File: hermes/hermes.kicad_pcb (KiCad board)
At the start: 2 copper layers, 46.5 x 74 mm, 9 parts, among them U1 AHT20, U2 XIAO-RP2040-DIP

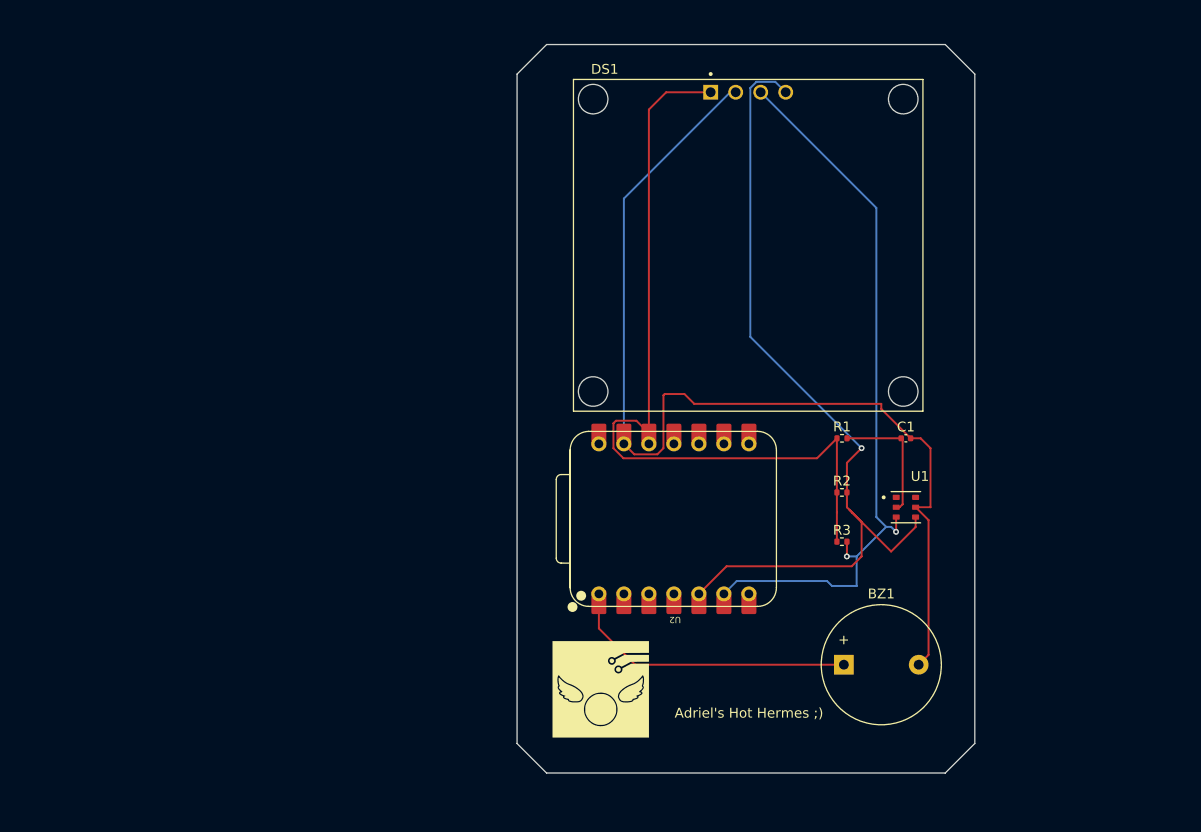
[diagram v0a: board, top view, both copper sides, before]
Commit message: changed some footprints
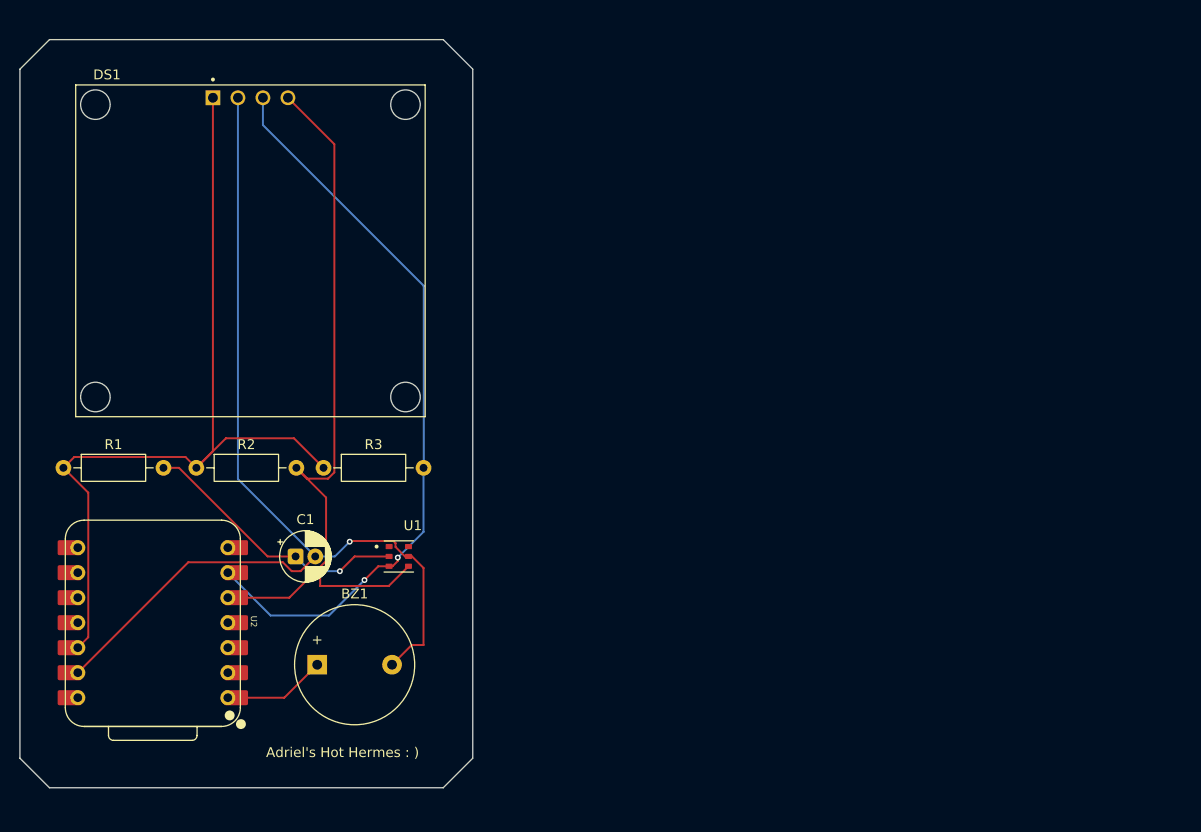
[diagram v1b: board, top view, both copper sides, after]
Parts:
- removed G***: LOGO, hermes:herm-22
- C1: footprint Capacitor_SMD:C_0402_1005Metric -> Capacitor_THT:CP_Radial_D5.0mm_P2.00mm
- R1, R2, R3: footprint Resistor_SMD:R_0402_1005Metric -> Resistor_THT:R_Axial_DIN0207_L6.3mm_D2.5mm_P10.16mm_Horizontal
- moved R1 79.1 mm to (69.4, 93.0)
- moved R2 65.6 mm to (82.9, 93.0)
- moved C1 63.2 mm to (93.0, 102.0)
- moved U2 54.0 mm to (78.5, 108.7), turned to -90 degrees
- moved BZ1 53.5 mm to (95.2, 113.0)
- moved R3 53.2 mm to (95.8, 93.0)
- moved U1 51.8 mm to (103.5, 102.0)
- moved DS1 50.6 mm to (88.4, 71.0)
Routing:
- net buzzer: track 29.9 -> 10.5 mm
- net Net-(U1-VDD): track 13.0 -> 27.9 mm, vias 0 -> 1
- net Net-(DS1-SDA): track 86.4 -> 77.5 mm, vias 1 -> 0
- net Net-(DS1-VDD): track 83.3 -> 87.9 mm
- net GND: track 105.1 -> 104.5 mm, vias 0 -> 1
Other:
- board size 46.5 x 74 mm -> 46 x 76 mm
- board text added: "Adriel's Hot Hermes : )"
- board text removed: "Adriel's Hot Hermes ;)"

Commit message: done
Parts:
- removed C1: 10u, Capacitor_THT:CP_Radial_D5.0mm_P2.00mm
- removed R1: 330, Resistor_THT:R_Axial_DIN0207_L6.3mm_D2.5mm_P10.16mm_Horizontal
- removed R2, R3: 4.7k, Resistor_THT:R_Axial_DIN0207_L6.3mm_D2.5mm_P10.16mm_Horizontal
- removed U1: AHT20, hermes-footprint:PSON100P300X300X110-6N
- added J1: Conn_01x04_Pin, Connector:FanPinHeader_1x04_P2.54mm_Vertical, F.Cu at (173.7, 98.8)
- moved U2 75.6 mm to (154.0, 112.6), turned to 180 degrees
- moved BZ1 75.5 mm to (170.7, 114.0)
- moved DS1 72.7 mm to (161.1, 67.7)
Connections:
- net Net-(DS1-SCK) renamed SCL
- net Net-(DS1-SDA) renamed SDA
- net Net-(DS1-VDD) renamed VDD
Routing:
- net Net-(U1-VDD): track 27.9 -> 0.00 mm, vias 1 -> 0
- net buzzer: track 10.5 -> 26.9 mm
- net VDD: track 87.9 -> 78.4 mm
- net GND: track 104.5 -> 98.2 mm
- net SDA: track 77.5 -> 82.3 mm
- net SCL: track 76.3 -> 80.6 mm, vias 2 -> 0
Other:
- board size 46 x 76 mm -> 43.5 x 80.5 mm
- board text removed: "Adriel's Hot Hermes : )"

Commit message: made a case
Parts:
- moved U2 3.13 mm to (151.0, 113.5)
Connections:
- J1 pad 1: VDD -> SDA
- J1 pad 2: GND -> SCL
- J1 pad 3: SCL -> GND
- J1 pad 4: SDA -> VDD
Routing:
- net SDA: track 82.3 -> 91.8 mm, vias 0 -> 1
- net buzzer: track 26.9 -> 34.4 mm
- net SCL: track 80.6 -> 87.4 mm, vias 0 -> 2
- net GND: track 98.2 -> 104.7 mm, vias 1 -> 3
- net VDD: track 78.4 -> 77.4 mm
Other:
- board size 43.5 x 80.5 mm -> 44 x 78 mm

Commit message: done again again
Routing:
- net VDD: track 77.4 -> 85.1 mm
- net SCL: track 87.4 -> 85.0 mm
- net buzzer: track 34.4 -> 32.6 mm
- net SDA: track 91.8 -> 90.2 mm
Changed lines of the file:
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@@
-	)
-	(segment
-		(start 159.82 52.105)
-		(end 159.82 83.274206)
-		(width 0.2)
-		(layer "F.Cu")
-		(net 1)
 	)
 	(segment
@@
 	)
 	(segment
+		(start 178.3 96.8)
+		(end 175.22 93.72)
+		(width 0.2)
+		(layer "F.Cu")
+		(net 1)
+	)
+	(segment
 		(start 159.045794 82.5)
 		(end 159.82 83.274206)
@@
 	)
 	(segment
-		(start 177.72 93.72)
-		(end 173.7 93.72)
+		(start 158.5 53.425)
+		(end 158.5 81.954206)
 		(width 0.2)
 		(layer "F.Cu")
@@
 	)
 	(segment
-		(start 178.3 94.3)
-		(end 177.72 93.72)
+		(start 175.22 93.72)
+		(end 173.7 93.72)
+		(width 0.2)
+		(layer "F.Cu")
+		(net 1)
+	)
+	(segment
+		(start 159.82 52.105)
+		(end 158.5 53.425)
+		(width 0.2)
+		(layer "F.Cu")
+		(net 1)
+	)
+	(segment
+		(start 178.3 114)
+		(end 178.3 96.8)
+		(width 0.2)
+		(layer "F.Cu")
+		(net 1)
+	)
+	(segment
+		(start 158.5 81.954206)
+		(end 159.82 83.274206)
 		(width 0.2)
 		(layer "F.Cu")
@@
 		(net 1)
 	)
-	(segment
-		(start 178.3 114)
-		(end 178.3 94.3)
-		(width 0.2)
-		(layer "F.Cu")
-		(net 1)
-	)
 	(via
 		(at 170 93.5)
@@
 	)
 	(segment
-		(start 143.5 114)
-		(end 143.38 114.12)
+		(start 143.38 117.12)
+		(end 143.38 121.12)
 		(width 0.2)
 		(layer "F.Cu")
@@
 	(segment
 		(start 170.7 114)
-		(end 143.5 114)
+		(end 146.5 114)
 		(width 0.2)
 		(layer "F.Cu")
@@
 	)
 	(segment
-		(start 143.38 114.12)
-		(end 143.38 121.12)
+		(start 146.5 114)
+		(end 143.38 117.12)
 		(width 0.2)
 		(layer "F.Cu")
@@
 	)
 	(segment
+		(start 164 53.005)
+		(end 164.9 52.105)
+		(width 0.2)
+		(layer "B.Cu")
+		(net 12)
+	)
+	(segment
+		(start 164.9 94.6)
+		(end 167 96.7)
+		(width 0.2)
+		(layer "B.Cu")
+		(net 12)
+	)
+	(segment
+		(start 164.9 94.6)
+		(end 164 93.7)
+		(width 0.2)
+		(layer "B.Cu")
+		(net 12)
+	)
+	(segment
 		(start 164.5 112.28)
 		(end 163.78 113)
@@
 	)
 	(segment
-		(start 153.54 113.54)
+		(start 164.9 94.6)
+		(end 164.5 95)
+		(width 0.2)
+		(layer "B.Cu")
+		(net 12)
+	)
+	(segment
+		(start 164 93.7)
+		(end 164 53.005)
+		(width 0.2)
+		(layer "B.Cu")
+		(net 12)
+	)
+	(segment
+		(start 163.78 113)
+		(end 157.5 113)
+		(width 0.2)
+		(layer "B.Cu")
+		(net 12)
+	)
+	(segment
+		(start 164.5 95)
+		(end 164.5 112.28)
+		(width 0.2)
+		(layer "B.Cu")
+		(net 12)
+	)
+	(segment
+		(start 153.54 116.96)
 		(end 153.54 121.12)
-		(width 0.2)
-		(layer "B.Cu")
-		(net 12)
-	)
-	(segment
-		(start 164.9 94.6)
-		(end 167 96.7)
-		(width 0.2)
-		(layer "B.Cu")
-		(net 12)
-	)
-	(segment
-		(start 153.5 113)
-		(end 153.5 113.5)
-		(width 0.2)
-		(layer "B.Cu")
-		(net 12)
-	)
-	(segment
-		(start 164.9 94.6)
-		(end 164.9 52.105)
-		(width 0.2)
-		(layer "B.Cu")
-		(net 12)
-	)
-	(segment
-		(start 163.78 113)
-		(end 153.5 113)
-		(width 0.2)
-		(layer "B.Cu")
-		(net 12)
-	)
-	(segment
-		(start 153.5 113.5)
-		(end 153.54 113.54)
-		(width 0.2)
-		(layer "B.Cu")
-		(net 12)
-	)
-	(segment
-		(start 164.5 112.28)
-		(end 164.5 95)
 		(width 0.2)
 		(layer "B.Cu")
@@
 	)
 	(segment
-		(start 164.5 95)
-		(end 164.9 94.6)
-		(width 0.2)
-		(layer "B.Cu")
-		(net 12)
+		(start 157.5 113)
+		(end 153.54 116.96)
+		(width 0.2)
+		(layer "B.Cu")
+		(net 12)
+	)
+	(segment
+		(start 157.45 88.45)
+		(end 160.5 91.5)
+		(width 0.2)
+		(layer "F.Cu")
+		(net 13)
+	)
+	(segment
+		(start 151 84)
+		(end 148.46 86.54)
+		(width 0.2)
+		(layer "F.Cu")
+		(net 13)
+	)
+	(segment
+		(start 156 81.1)
+		(end 157.45 82.55)
+		(width 0.2)
+		(layer "F.Cu")
+		(net 13)
 	)
 	(segment
 		(start 157.45 82.55)
-		(end 165.9 91)
-		(width 0.2)
-		(layer "F.Cu")
-		(net 13)
-	)
-	(segment
-		(start 157.45 82.55)
-		(end 148.46 91.54)
+		(end 157.45 88.45)
+		(width 0.2)
+		(layer "F.Cu")
+		(net 13)
+	)
+	(segment
+		(start 156 84)
+		(end 151 84)
 		(width 0.2)
 		(layer "F.Cu")
@@
 	)
 	(segment
-		(start 148.46 91.54)
+		(start 156 53.385)
+		(end 156 81.1)
+		(width 0.2)
+		(layer "F.Cu")
+		(net 13)
+	)
+	(segment
+		(start 167.86 91.5)
+		(end 168.18 91.18)
+		(width 0.2)
+		(layer "F.Cu")
+		(net 13)
+	)
+	(segment
+		(start 157.45 82.55)
+		(end 156 84)
+		(width 0.2)
+		(layer "F.Cu")
+		(net 13)
+	)
+	(segment
+		(start 157.28 52.105)
+		(end 156 53.385)
+		(width 0.2)
+		(layer "F.Cu")
+		(net 13)
+	)
+	(segment
+		(start 160.5 91.5)
+		(end 167.86 91.5)
+		(width 0.2)
+		(layer "F.Cu")
+		(net 13)
+	)
+	(segment
+		(start 148.46 86.54)
 		(end 148.46 105.88)
 		(width 0.2)
@@
 	)
 	(segment
-		(start 157.28 82.38)
-		(end 157.45 82.55)
-		(width 0.2)
-		(layer "F.Cu")
-		(net 13)
-	)
-	(segment
-		(start 168 91)
-		(end 168.18 91.18)
-		(width 0.2)
-		(layer "F.Cu")
-		(net 13)
-	)
-	(segment
-		(start 157.28 52.105)
-		(end 157.28 82.38)
-		(width 0.2)
-		(layer "F.Cu")
-		(net 13)
-	)
-	(segment
-		(start 165.9 91)
-		(end 168 91)
-		(width 0.2)
-		(layer "F.Cu")
-		(net 13)
+		(start 162.36 52.105)
+		(end 161.5 52.965)
+		(width 0.2)
+		(layer "F.Cu")
+		(net 14)
 	)
 	(segment
@@
 	)
 	(segment
-		(start 162.36 52.105)
+		(start 162.36 82.38)
+		(end 162.36 83.86)
+		(width 0.2)
+		(layer "F.Cu")
+		(net 14)
+	)
+	(segment
+		(start 161.5 52.965)
+		(end 161.5 81.52)
+		(width 0.2)
+		(layer "F.Cu")
+		(net 14)
+	)
+	(segment
+		(start 161.5 81.52)
 		(end 162.36 82.38)
 		(width 0.2)
@@
 	)
 	(segment
-		(start 162.36 82.38)
-		(end 162.36 83.86)
-		(width 0.2)
-		(layer "F.Cu")
-		(net 14)
-	)
-	(segment
 		(start 170 96.5)
 		(end 170.24 96.26)
@@
 	)
 	(segment
+		(start 158 116.5)
+		(end 156.08 118.42)
+		(width 0.2)
+		(layer "B.Cu")
+		(net 14)
+	)
+	(segment
 		(start 168.5 97)
 		(end 169 96.5)
@@
 	)
 	(segment
-		(start 168.5 97)
-		(end 168.5 110.82)
-		(width 0.2)
-		(layer "B.Cu")
-		(net 14)
-	)
-	(segment
-		(start 163.5 114.5)
-		(end 163.5 116.5)
-		(width 0.2)
-		(layer "B.Cu")
-		(net 14)
-	)
-	(segment
-		(start 163.5 116.5)
-		(end 156 116.5)
-		(width 0.2)
-		(layer "B.Cu")
-		(net 14)
-	)
-	(segment
 		(start 169 96.5)
 		(end 170 96.5)
@@
 	)
 	(segment
-		(start 168.5 110.82)
-		(end 167.18 110.82)
+		(start 156.08 118.42)
+		(end 156.08 121.12)
+		(width 0.2)
+		(layer "B.Cu")
+		(net 14)
+	)
+	(segment
+		(start 168.5 97)
+		(end 168.5 109.5)
 		(width 0.2)
 		(layer "B.Cu")
@@
 	)
 	(segment
-		(start 156 116.5)
-		(end 156.08 116.58)
+		(start 161.5 116.5)
+		(end 158 116.5)
 		(width 0.2)
 		(layer "B.Cu")
@@
 	)
 	(segment
-		(start 156.08 116.58)
-		(end 156.08 121.12)
-		(width 0.2)
-		(layer "B.Cu")
-		(net 14)
-	)
-	(segment
-		(start 167.18 110.82)
-		(end 163.5 114.5)
-		(width 0.2)
-		(layer "B.Cu")
+		(start 168.5 109.5)
+		(end 161.5 116.5)
+		(width 0.2)
+		(layer "B.Cu")
